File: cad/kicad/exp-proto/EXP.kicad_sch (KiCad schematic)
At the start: 23 parts, among them J1 IN, J2 IN, J3 OUT, J4 OUT, J5 On, J6 In, J7 KEYPAD, J8 INTR, U1 74F138, U2 74F138, U3 74F574, U4 74F174, U5 74F244, U6 MCP1702-5002E

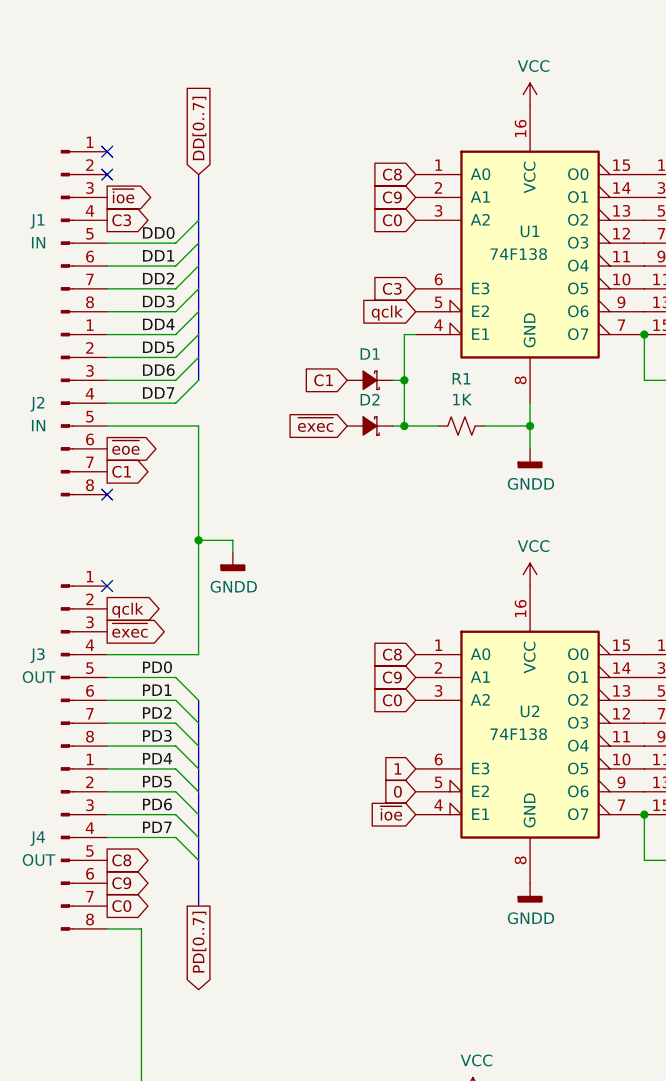
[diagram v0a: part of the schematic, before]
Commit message: update old C-reg labels
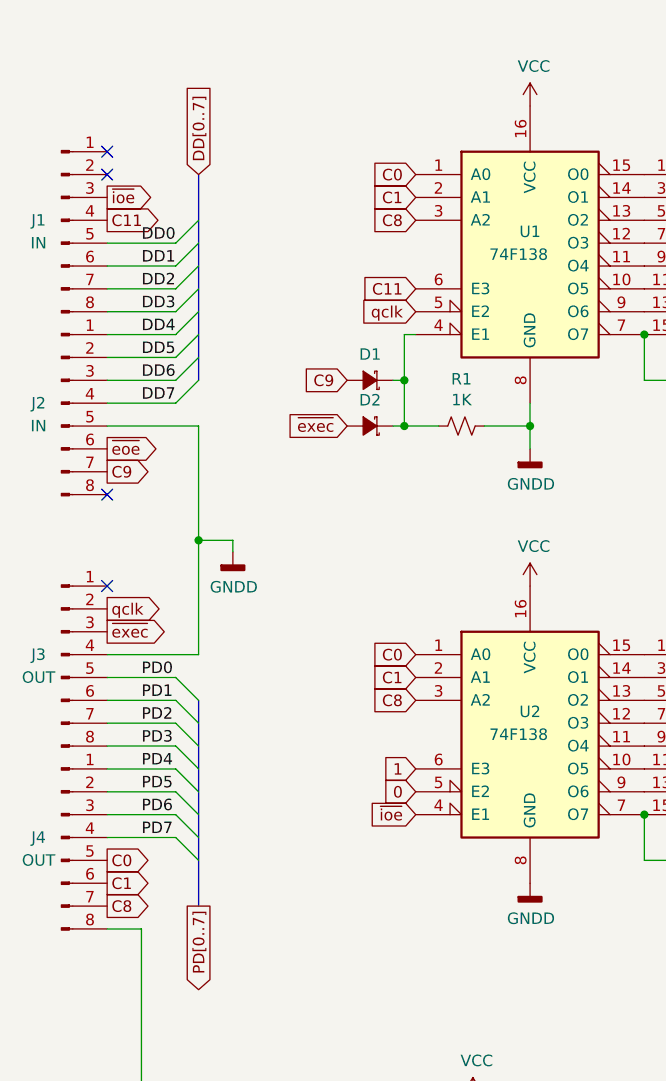
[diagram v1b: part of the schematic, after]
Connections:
- net C0: now also J4.5 (Pin_5), U1.1 (A0), U2.1 (A0); no longer J4.7 (Pin_7), U1.3 (A2), U2.3 (A2)
- net C1: now also J4.6 (Pin_6), U1.2 (A1), U2.2 (A1); no longer D1.2 (A), J2.7 (Pin_7)
- net C8: now also J4.7 (Pin_7), U1.3 (A2), U2.3 (A2); no longer J4.5 (Pin_5), U1.1 (A0), U2.1 (A0)
- net C9: now also D1.2 (A), J2.7 (Pin_7); no longer J4.6 (Pin_6), U1.2 (A1), U2.2 (A1)
- net C3 renamed C11
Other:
- company: Solid-state Machines -> Solid State Machines LLC
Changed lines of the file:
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@@
   (title_block
     (title "Novasaur Expansion Prototype")
-    (date "2022-05-19")
+    (date "2023-05-22")
     (rev "3")
-    (company "Solid-state Machines")
-    (comment 1 "Copyright (c) 2022")
+    (company "Solid State Machines LLC")
+    (comment 1 "Copyright (c) 2023")
   )
   (junction (at 41.91 76.2) (diameter 0) (color 0 0 0 0)
@@
     (effects (font (size 1.27 1.27)) (justify left bottom))
   )
-  (global_label "C1" (shape output) (at 31.75 68.58 0) (fields_autoplaced)
-    (effects (font (size 1.27 1.27)) (justify left))
-    (property "Intersheet References" "${INTERSHEET_REFS}" (id 0) (at 0 0 0)
-      (effects (font (size 1.27 1.27)) hide)
-    )
-  )
-  (global_label "C8" (shape input) (at 66.04 35.56 180) (fields_autoplaced)
-    (effects (font (size 1.27 1.27)) (justify right))
-    (property "Intersheet References" "${INTERSHEET_REFS}" (id 0) (at 0 0 0)
-      (effects (font (size 1.27 1.27)) hide)
-    )
-  )
-  (global_label "C3" (shape input) (at 66.04 48.26 180) (fields_autoplaced)
-    (effects (font (size 1.27 1.27)) (justify right))
-    (property "Intersheet References" "${INTERSHEET_REFS}" (id 0) (at 0 0 0)
-      (effects (font (size 1.27 1.27)) hide)
+  (global_label "C9" (shape output) (at 31.75 68.58 0) (fields_autoplaced)
+    (effects (font (size 1.27 1.27)) (justify left))
+    (property "Intersheet References" "${INTERSHEET_REFS}" (id 0) (at 36.5537 68.5006 0)
+      (effects (font (size 1.27 1.27)) (justify left) hide)
+    )
+  )
+  (global_label "C0" (shape input) (at 66.04 35.56 180) (fields_autoplaced)
+    (effects (font (size 1.27 1.27)) (justify right))
+    (property "Intersheet References" "${INTERSHEET_REFS}" (id 0) (at 61.2363 35.4806 0)
+      (effects (font (size 1.27 1.27)) (justify right) hide)
+    )
+  )
+  (global_label "C11" (shape input) (at 66.04 48.26 180) (fields_autoplaced)
+    (effects (font (size 1.27 1.27)) (justify right))
+    (property "Intersheet References" "${INTERSHEET_REFS}" (id 0) (at 60.0268 48.1806 0)
+      (effects (font (size 1.27 1.27)) (justify right) hide)
     )
   )
@@
     )
   )
-  (global_label "C8" (shape input) (at 66.04 88.9 180) (fields_autoplaced)
-    (effects (font (size 1.27 1.27)) (justify right))
-    (property "Intersheet References" "${INTERSHEET_REFS}" (id 0) (at 0 0 0)
-      (effects (font (size 1.27 1.27)) hide)
+  (global_label "C0" (shape input) (at 66.04 88.9 180) (fields_autoplaced)
+    (effects (font (size 1.27 1.27)) (justify right))
+    (property "Intersheet References" "${INTERSHEET_REFS}" (id 0) (at 61.2363 88.8206 0)
+      (effects (font (size 1.27 1.27)) (justify right) hide)
     )
   )
@@
     )
   )
-  (global_label "C8" (shape output) (at 31.75 111.76 0) (fields_autoplaced)
-    (effects (font (size 1.27 1.27)) (justify left))
-    (property "Intersheet References" "${INTERSHEET_REFS}" (id 0) (at 0 0 0)
-      (effects (font (size 1.27 1.27)) hide)
+  (global_label "C0" (shape output) (at 31.75 111.76 0) (fields_autoplaced)
+    (effects (font (size 1.27 1.27)) (justify left))
+    (property "Intersheet References" "${INTERSHEET_REFS}" (id 0) (at 36.5537 111.6806 0)
+      (effects (font (size 1.27 1.27)) (justify left) hide)
     )
   )
@@
     )
   )
-  (global_label "C9" (shape input) (at 66.04 91.44 180) (fields_autoplaced)
-    (effects (font (size 1.27 1.27)) (justify right))
-    (property "Intersheet References" "${INTERSHEET_REFS}" (id 0) (at 0 0 0)
-      (effects (font (size 1.27 1.27)) hide)
-    )
-  )
-  (global_label "C0" (shape output) (at 31.75 116.84 0) (fields_autoplaced)
-    (effects (font (size 1.27 1.27)) (justify left))
-    (property "Intersheet References" "${INTERSHEET_REFS}" (id 0) (at 0 0 0)
-      (effects (font (size 1.27 1.27)) hide)
+  (global_label "C1" (shape input) (at 66.04 91.44 180) (fields_autoplaced)
+    (effects (font (size 1.27 1.27)) (justify right))
+    (property "Intersheet References" "${INTERSHEET_REFS}" (id 0) (at 61.2363 91.3606 0)
+      (effects (font (size 1.27 1.27)) (justify right) hide)
+    )
+  )
+  (global_label "C8" (shape output) (at 31.75 116.84 0) (fields_autoplaced)
+    (effects (font (size 1.27 1.27)) (justify left))
+    (property "Intersheet References" "${INTERSHEET_REFS}" (id 0) (at 36.5537 116.7606 0)
+      (effects (font (size 1.27 1.27)) (justify left) hide)
     )
   )
@@
     )
   )
-  (global_label "C0" (shape input) (at 66.04 93.98 180) (fields_autoplaced)
-    (effects (font (size 1.27 1.27)) (justify right))
-    (property "Intersheet References" "${INTERSHEET_REFS}" (id 0) (at 0 0 0)
-      (effects (font (size 1.27 1.27)) hide)
+  (global_label "C8" (shape input) (at 66.04 93.98 180) (fields_autoplaced)
+    (effects (font (size 1.27 1.27)) (justify right))
+    (property "Intersheet References" "${INTERSHEET_REFS}" (id 0) (at 61.2363 93.9006 0)
+      (effects (font (size 1.27 1.27)) (justify right) hide)
     )
   )
@@
     )
   )
-  (global_label "C3" (shape output) (at 31.75 40.64 0) (fields_autoplaced)
-    (effects (font (size 1.27 1.27)) (justify left))
-    (property "Intersheet References" "${INTERSHEET_REFS}" (id 0) (at 0 0 0)
-      (effects (font (size 1.27 1.27)) hide)
-    )
-  )
-  (global_label "C9" (shape output) (at 31.75 114.3 0) (fields_autoplaced)
-    (effects (font (size 1.27 1.27)) (justify left))
-    (property "Intersheet References" "${INTERSHEET_REFS}" (id 0) (at 0 0 0)
-      (effects (font (size 1.27 1.27)) hide)
+  (global_label "C11" (shape output) (at 31.75 40.64 0) (fields_autoplaced)
+    (effects (font (size 1.27 1.27)) (justify left))
+    (property "Intersheet References" "${INTERSHEET_REFS}" (id 0) (at 37.7632 40.5606 0)
+      (effects (font (size 1.27 1.27)) (justify left) hide)
+    )
+  )
+  (global_label "C1" (shape output) (at 31.75 114.3 0) (fields_autoplaced)
+    (effects (font (size 1.27 1.27)) (justify left))
+    (property "Intersheet References" "${INTERSHEET_REFS}" (id 0) (at 36.5537 114.2206 0)
+      (effects (font (size 1.27 1.27)) (justify left) hide)
     )
   )
@@
     )
   )
-  (global_label "C0" (shape input) (at 66.04 40.64 180) (fields_autoplaced)
-    (effects (font (size 1.27 1.27)) (justify right))
-    (property "Intersheet References" "${INTERSHEET_REFS}" (id 0) (at 0 0 0)
-      (effects (font (size 1.27 1.27)) hide)
-    )
-  )
-  (global_label "C9" (shape input) (at 66.04 38.1 180) (fields_autoplaced)
-    (effects (font (size 1.27 1.27)) (justify right))
-    (property "Intersheet References" "${INTERSHEET_REFS}" (id 0) (at 0 0 0)
-      (effects (font (size 1.27 1.27)) hide)
-    )
-  )
-  (global_label "C1" (shape input) (at 58.42 58.42 180) (fields_autoplaced)
-    (effects (font (size 1.27 1.27)) (justify right))
-    (property "Intersheet References" "${INTERSHEET_REFS}" (id 0) (at 0 0 0)
-      (effects (font (size 1.27 1.27)) hide)
-    )
-  )
+  (global_label "C8" (shape input) (at 66.04 40.64 180) (fields_autoplaced)
+    (effects (font (size 1.27 1.27)) (justify right))
+    (property "Intersheet References" "${INTERSHEET_REFS}" (id 0) (at 61.2363 40.5606 0)
+      (effects (font (size 1.27 1.27)) (justify right) hide)
+    )
+  )
+  (global_label "C1" (shape input) (at 66.04 38.1 180) (fields_autoplaced)
+    (effects (font (size 1.27 1.27)) (justify right))
+    (property "Intersheet References" "${INTERSHEET_REFS}" (id 0) (at 61.2363 38.0206 0)
+      (effects (font (size 1.27 1.27)) (justify right) hide)
+    )
+  )
+  (global_label "C9" (shape input) (at 58.42 58.42 180) (fields_autoplaced)
+    (effects (font (size 1.27 1.27)) (justify right))
+    (property "Intersheet References" "${INTERSHEET_REFS}" (id 0) (at 53.6163 58.3406 0)
+      (effects (font (size 1.27 1.27)) (justify right) hide)
+    )
+  )
